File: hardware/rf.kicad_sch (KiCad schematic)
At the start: 6 parts, among them U1 SN74CBT3253, U2 XLV320ADC6120IRTER, Y1 Si5351A-B-GT

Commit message: amp and audio
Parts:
- added C21, C22: 100nF, Capacitor_SMD:C_0805_2012Metric_Pad1.18x1.45mm_HandSolder, symbol Device:C
- added FB3: GZ2012D601TF, Inductor_SMD:L_0805_2012Metric_Pad1.05x1.20mm_HandSolder, symbol Device:FerriteBead_Small
- added U6: BGA2817, Package_TO_SOT_SMD:SOT-363_SC-70-6, symbol RF_Amplifier:BGA2817
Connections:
- net +3.3VA: now also FB3.1
- net GND: now also C22.1, U6.2 (G), U6.4 (G), U6.5 (G)
- net at U1.9 (2A): now also C21.1
- new net: C22.2, FB3.2, U6.1 (Vcc)
- new net: C21.2, U6.3
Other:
- moved on the sheet: C17, C18, FB2, U1, U2, Y1

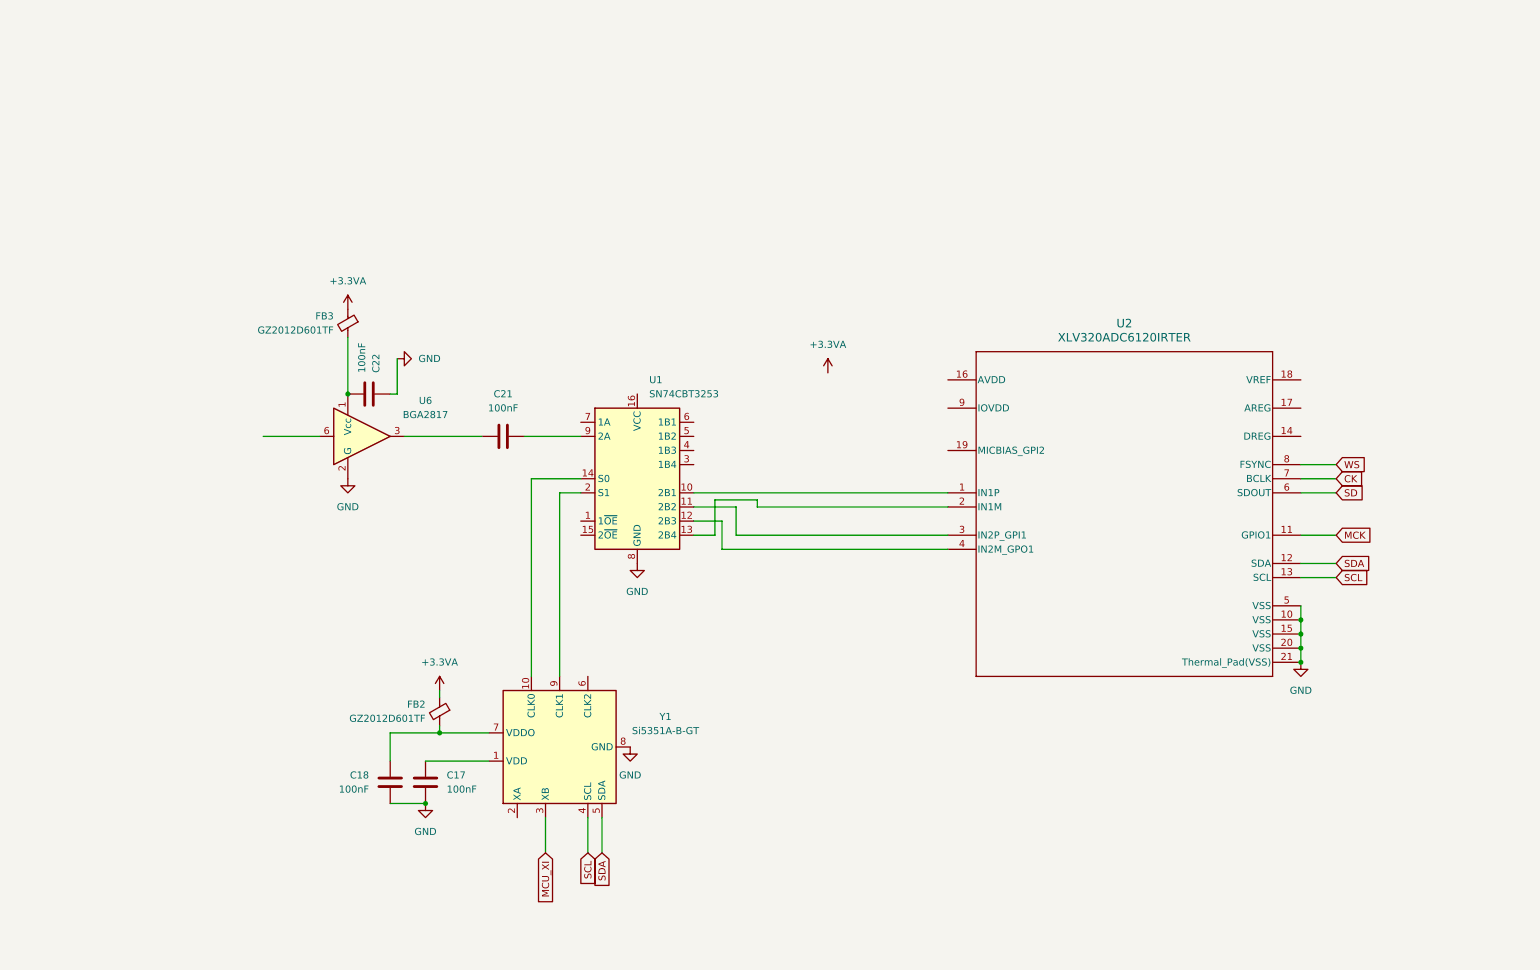
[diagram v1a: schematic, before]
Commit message: initial component layout
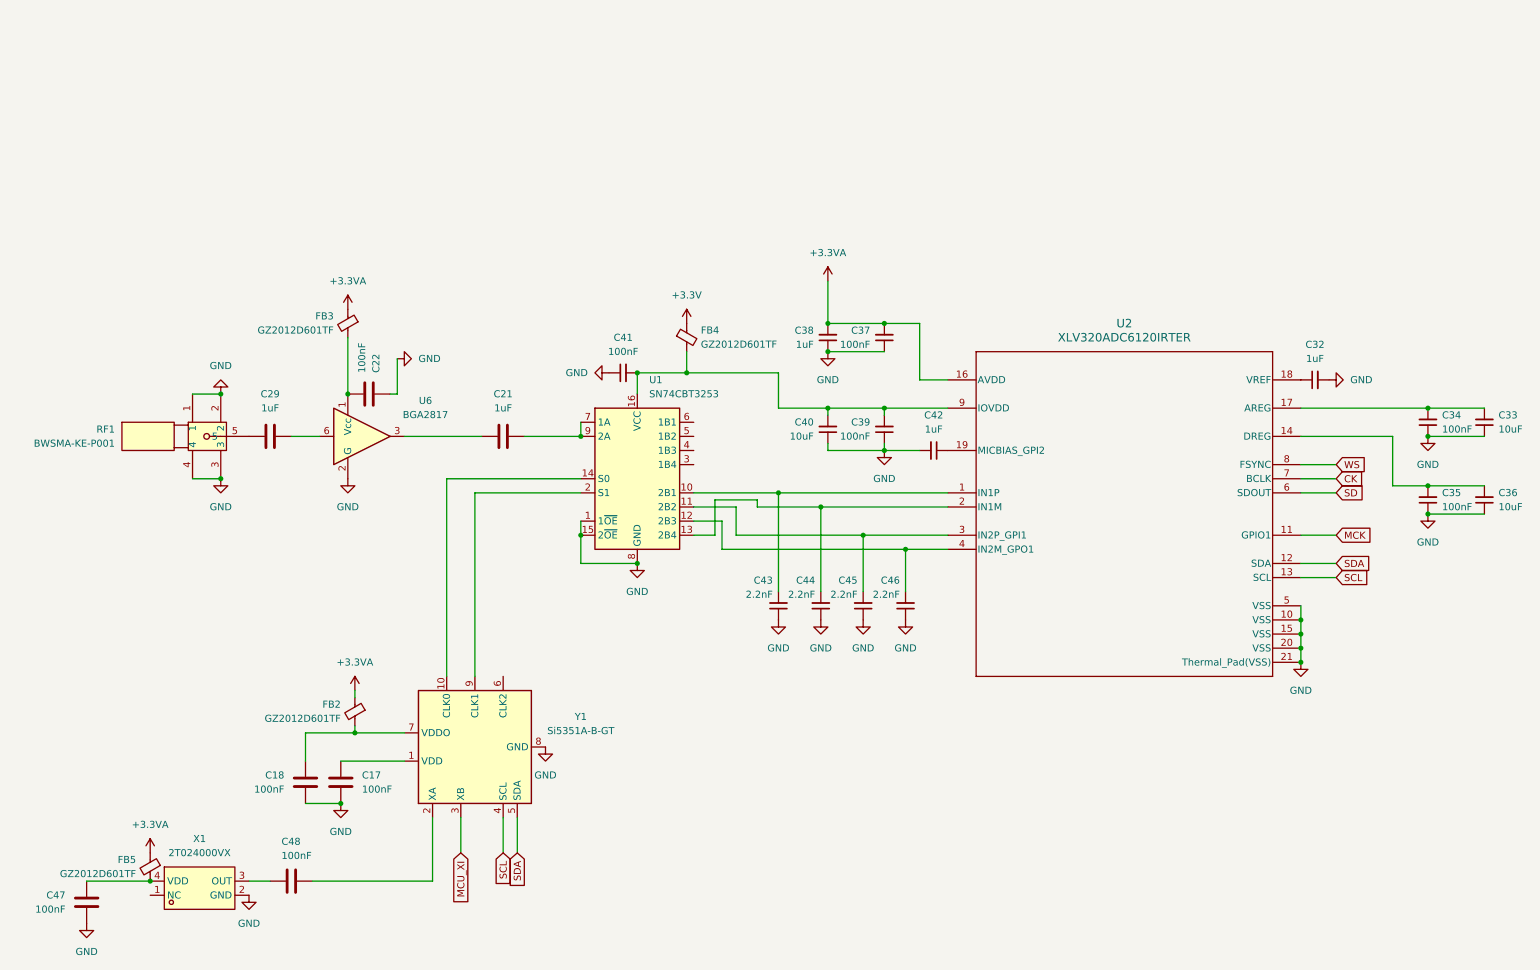
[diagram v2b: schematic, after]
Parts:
- added C29: 1uF, Capacitor_SMD:C_0805_2012Metric_Pad1.18x1.45mm_HandSolder, symbol Device:C
- added C32, C38, C42: 1uF, Capacitor_SMD:C_0805_2012Metric_Pad1.18x1.45mm_HandSolder, symbol Device:C_Small
- added C33, C36, C40: 10uF, Capacitor_SMD:C_0805_2012Metric_Pad1.18x1.45mm_HandSolder, symbol Device:C_Small
- added C34, C35, C37, C39, C41: 100nF, Capacitor_SMD:C_0805_2012Metric_Pad1.18x1.45mm_HandSolder, symbol Device:C_Small
- added C43, C44, C45, C46: 2.2nF, Capacitor_SMD:C_0805_2012Metric_Pad1.18x1.45mm_HandSolder, symbol Device:C_Small
- added C47, C48: 100nF, Capacitor_SMD:C_0805_2012Metric_Pad1.18x1.45mm_HandSolder, symbol Device:C
- added FB4, FB5: GZ2012D601TF, Inductor_SMD:L_0805_2012Metric_Pad1.05x1.20mm_HandSolder, symbol Device:FerriteBead_Small
- added RF1: BWSMA-KE-P001, easyeda:SMA-SMD_BWSMA-KE-P001, symbol easyeda:BWSMA-KE-P001
- added X1: 2T024000VX, easyeda:OSC-SMD_4P-L2.5-W2.0-BL_X1G0054210307, symbol easyeda:2T024000VX
- C21: value 100nF -> 1uF
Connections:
- net +3.3VA: now also U2.16 (AVDD), C37.2, C38.2, FB5.1
- net GND: now also U1.1 (1~{OE}), U1.15 (2~{OE}), C32.2, C33.1, C34.1, C35.1, C36.1, C37.1, C38.1, C39.1, C40.1, C41.1, C42.2, C43.1, C44.1, C45.1, C46.1, C47.2, RF1.1, RF1.2, RF1.3, RF1.4, X1.2 (GND)
- net at Y1.2 (XA): now also C48.1
- net at U6.6: now also C29.1
- net at U1.10 (2B1), U2.1 (IN1P): now also C43.2
- net at U1.11 (2B2), U2.3 (IN2P_GPI1): now also C45.2
- net at U1.12 (2B3), U2.4 (IN2M_GPO1): now also C46.2
- net at U1.13 (2B4), U2.2 (IN1M): now also C44.2
- net at U1.16 (VCC): now also U2.9 (IOVDD), C39.2, C40.2, C41.2, FB4.2
- net at U1.7 (1A): now also C21.1, U1.9 (2A)
- net at U2.14 (DREG): now also C35.2, C36.2
- net at U2.17 (AREG): now also C33.2, C34.2
- net at U2.18 (VREF): now also C32.1
- net at U2.19 (MICBIAS_GPI2): now also C42.1
- new net: C29.2, RF1.5
- new net: C47.1, FB5.2, X1.4 (VDD)
- new net: C48.2, X1.3 (OUT)
- new net +3.3V: FB4.1
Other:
- moved on the sheet: C17, C18, FB2, Y1

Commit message: hardware fix: MCO MCK + MS5351 VDD
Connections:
- net +3.3V: now also C17.2, Y1.1 (VDD)
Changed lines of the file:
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@@
 	)
 	(junction
+		(at 80.01 157.48)
+		(diameter 0)
+		(color 0 0 0 0)
+	)
+	(junction
 		(at 157.48 78.74)
 		(diameter 0)
@@
 	(wire
 		(pts
-			(xy 69.85 157.48) (xy 81.28 157.48)
+			(xy 69.85 157.48) (xy 80.01 157.48)
 		)
 		(stroke
@@
 	(wire
 		(pts
+			(xy 80.01 157.48) (xy 81.28 157.48)
+		)
+		(stroke
+			(width 0)
+			(type default)
+		)
+	)
+	(wire
+		(pts
 			(xy 24.13 179.07) (xy 35.56 179.07)
 		)
@@
 		)
 	)
+	(wire
+		(pts
+			(xy 80.01 157.48) (xy 80.01 165.1)
+		)
+		(stroke
+			(width 0)
+			(type default)
+		)
+	)
 	(global_label "WS"
 		(shape input)
@@
 					(unit 1)
 				)
+			)
+		)
+	)
+	(symbol
+		(lib_id "power:+3.3V")
+		(at 80.01 165.1 180)
+		(unit 1)
+		(exclude_from_sim no)
+		(in_bom yes)
+		(on_board yes)
+		(dnp no)
+		(fields_autoplaced yes)
+		(property "Reference" "#PWR082"
+			(at 80.01 161.29 0)
+			(effects
+				(font
+					(size 1.27 1.27)
+				)
+				(hide yes)
+			)
+		)
+		(property "Value" "+3.3V"
+			(at 80.01 170.18 0)
+			(effects
+				(font
+					(size 1.27 1.27)
+				)
+			)
+		)
+		(property "Footprint" ""
+			(at 80.01 165.1 0)
+			(effects
+				(font
+					(size 1.27 1.27)
+				)
+				(hide yes)
+			)
+		)
+		(property "Datasheet" ""
+			(at 80.01 165.1 0)
+			(effects
+				(font
+					(size 1.27 1.27)
+				)
+				(hide yes)
+			)
+		)
+		(property "Description" "Power symbol creates a global label with name \"+3.3V\""
+			(at 80.01 165.1 0)
+			(effects
+				(font
+					(size 1.27 1.27)
+				)
+				(hide yes)
+			)
+		)
+		(pin "1"
+		)
+		(instances
+			(project "hfsdr"
+				(path "/a11445ed-c3bd-4d1c-a039-1c09b0dceab8/53c9ae5e-dd7f-4449-b148-e9a80e46b47d"
+					(reference "#PWR082")
+					(unit 1)
+				)

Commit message: Ready for production
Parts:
- C?: renamed from C43; value 2.2nF -> 10nF
- C?: renamed from C45; value 2.2nF -> 10nF
- C?: renamed from C46; value 2.2nF -> 10nF
- C?: renamed from C44; value 2.2nF -> 10nF
- U?: renamed from U1; value SN74CBT3253 -> SN74CBTLV3253
- renumbered C29 to C?, C41 to C?, C47 to C?, C32 to C?, C40 to C?, C36 to C?, C17 to C?, C35 to C?, C48 to C?, C39 to C?, C22 to C?, C18 to C?, C38 to C?, C37 to C?, C33 to C?, C42 to C?, C21 to C?, C34 to C?, FB2 to FB?, FB3 to FB?, FB5 to FB?, FB4 to FB?, RF1 to RF?, U6 to U?, U2 to U?, X1 to X?, Y1 to Y?

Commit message: Protection diode
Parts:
- added D5: BAV99, Package_TO_SOT_SMD:SOT-23, symbol Diode:BAV99
- gave numbers to parts that had none: 32
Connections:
- net GND: now also D5.1 (K), D5.2 (A)
- net at C29.2, RF1.5: now also D5.3 (K)
